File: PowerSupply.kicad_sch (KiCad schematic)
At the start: 23 parts, among them J1 Barrel_Jack, SW1 SW_SPST, U1 LM7812_TO220, U2 LM7912_TO220, U3 LM7805_TO220

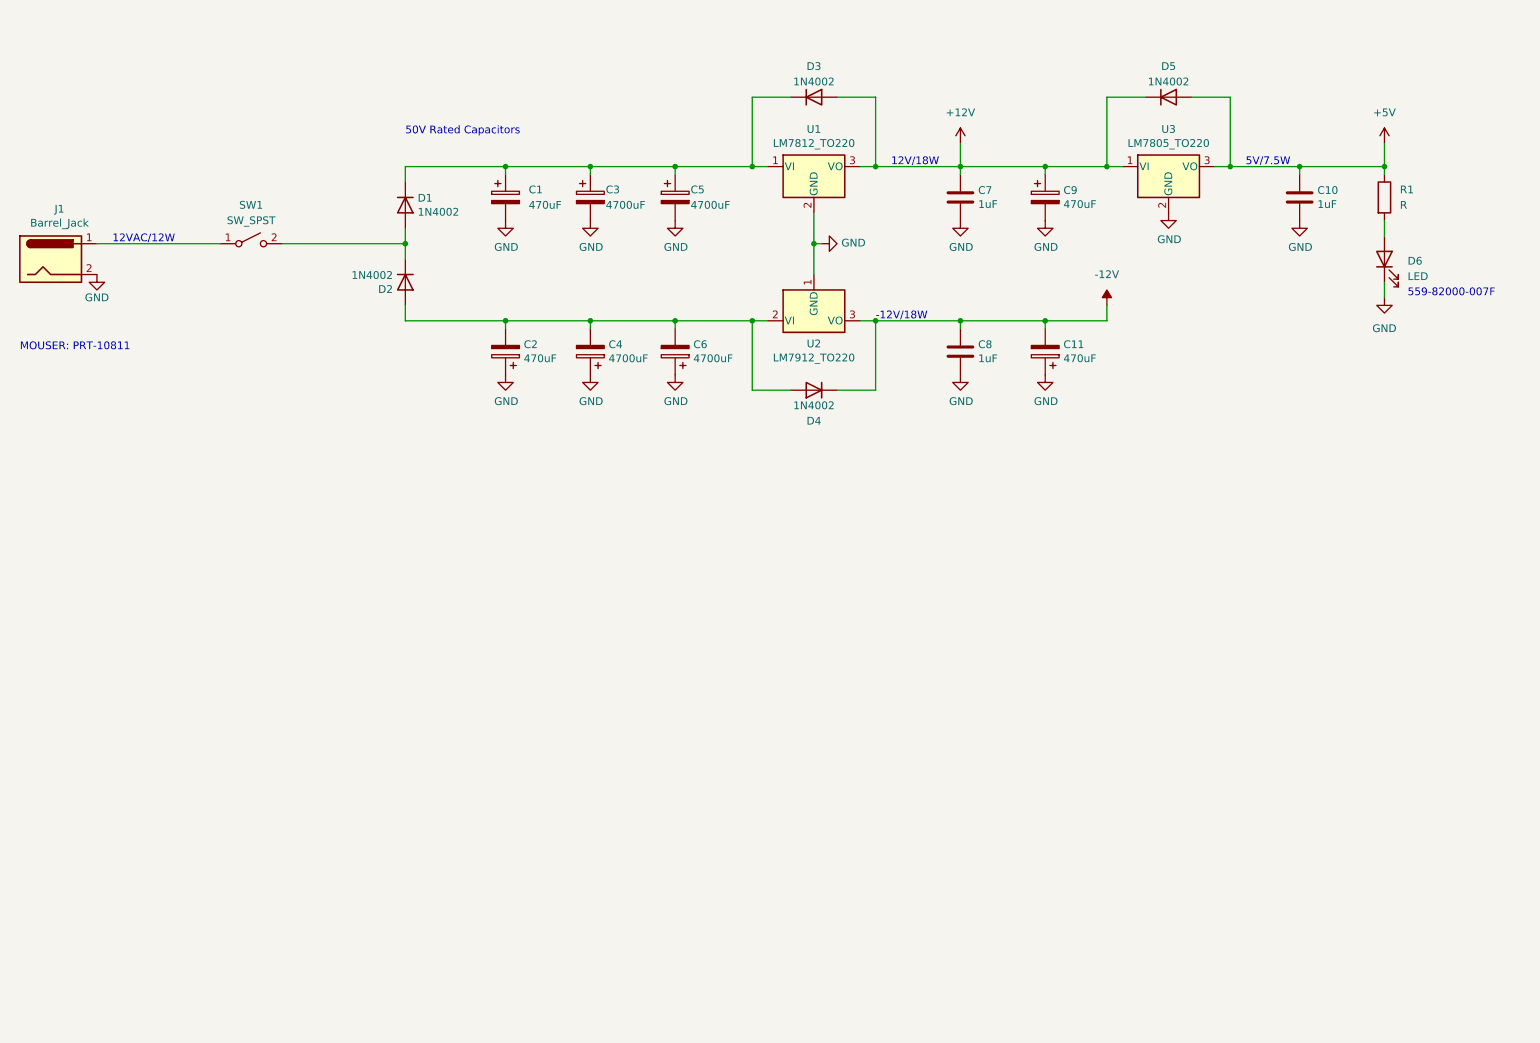
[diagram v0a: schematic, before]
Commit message: more uFs
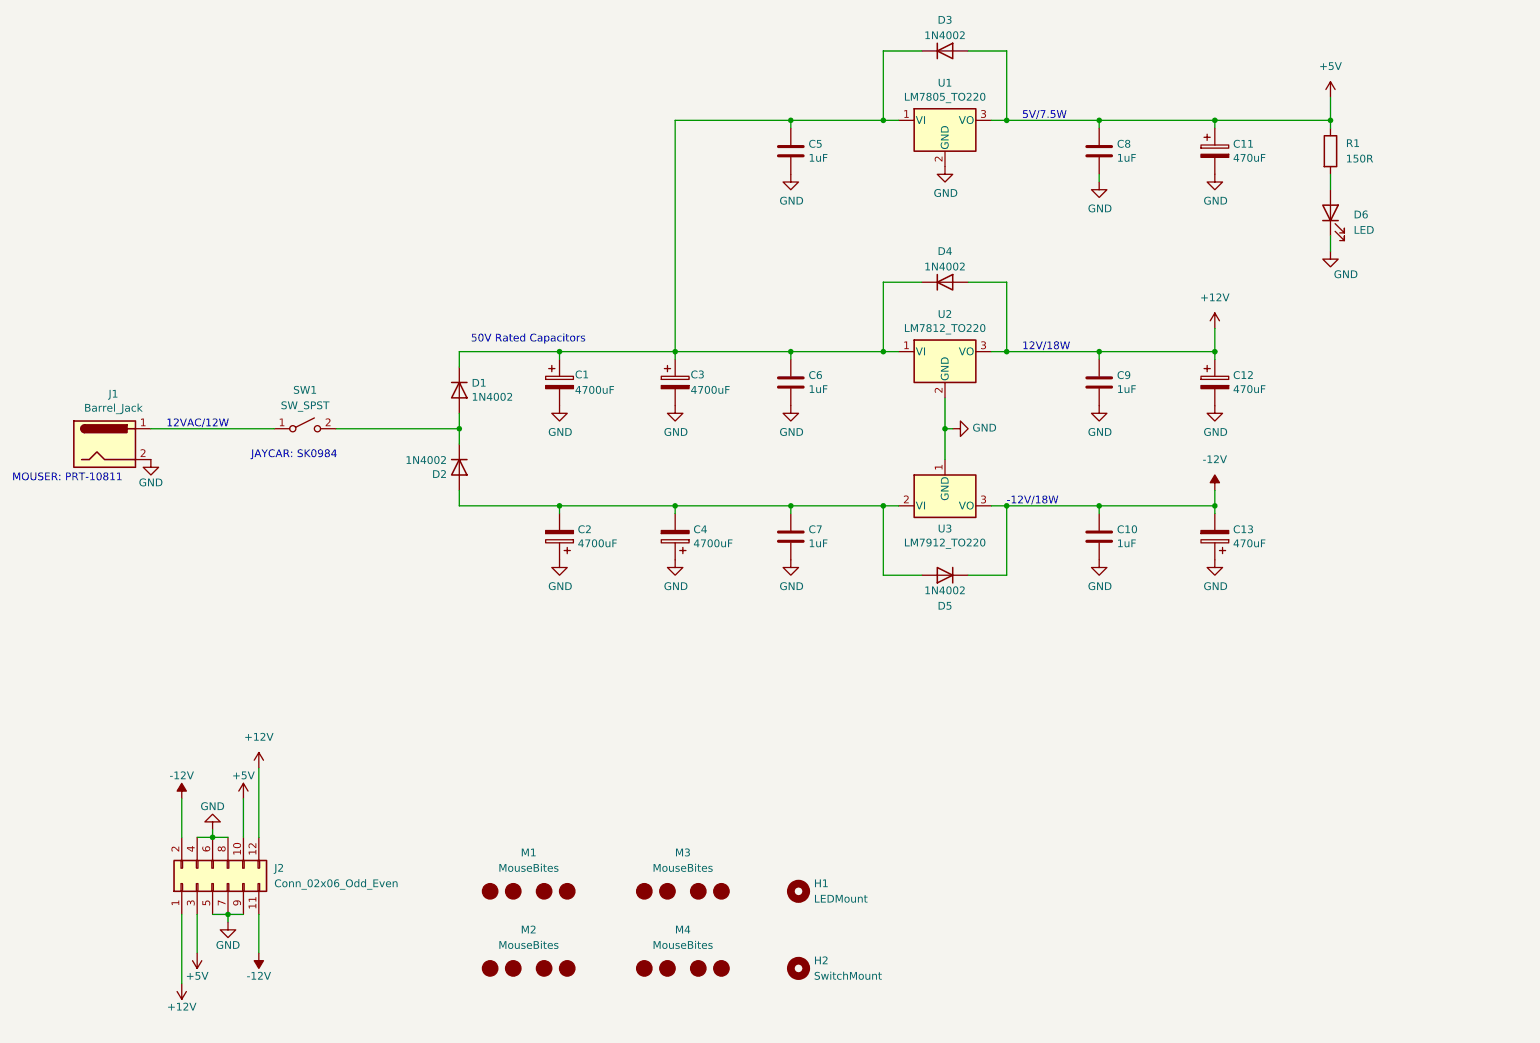
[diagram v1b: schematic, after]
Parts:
- removed C1: 470uF, Capacitor_THT:CP_Radial_D10.0mm_P5.00mm, symbol Device:CP
- removed C5, C6: 4700uF, Capacitor_THT:CP_Radial_D22.0mm_P10.00mm_SnapIn, symbol Device:CP
- added C11: 470uF, Capacitor_THT:CP_Radial_D10.0mm_P5.00mm, symbol Device:CP
- added C3: 4700uF, Capacitor_THT:CP_Radial_D22.0mm_P10.00mm_SnapIn, symbol Device:CP
- added C5, C6, C7: 1uF, Capacitor_SMD:C_0805_2012Metric_Pad1.18x1.45mm_HandSolder, symbol Device:C
- added H1: LEDMount, Synth:PowerLEDMount, symbol Mechanical:MountingHole
- added H2: SwitchMount, Synth:SwitchMount, symbol Mechanical:MountingHole
- added J2: Conn_02x06_Odd_Even, Connector_IDC:IDC-Header_2x06_P2.54mm_Vertical, symbol Connector_Generic:Conn_02x06_Odd_Even
- added M1, M2, M3, M4: MouseBites, Panelization:mouse-bite-5mm-slot, symbol Synth:MouseBites
- C2: value 470uF -> 4700uF; footprint Capacitor_THT:CP_Radial_D10.0mm_P5.00mm -> Capacitor_THT:CP_Radial_D22.0mm_P10.00mm_SnapIn
- J1: footprint (none) -> Synth:BarrelJack
- R1: value R -> 150R
- renumbered C3 to C1, C8 to C10, C9 to C12, C11 to C13, C10 to C8, C7 to C9, D5 to D3, D3 to D4, D4 to D5, U3 to U1, U1 to U2, U2 to U3
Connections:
- net +12V: now also J2.1 (Pin_1), J2.12 (Pin_12); no longer D3.1 (K), U1.1 (VI)
- net +5V: now also C11.1, J2.10 (Pin_10), J2.3 (Pin_3)
- net -12V: now also J2.11 (Pin_11), J2.2 (Pin_2)
- net GND: now also C11.2, C3.2, C5.2, C6.2, C7.2, J2.4 (Pin_4), J2.5 (Pin_5), J2.6 (Pin_6), J2.7 (Pin_7), J2.8 (Pin_8), J2.9 (Pin_9)
- net at C1.1, D1.1 (K), D4.1 (K)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: now also D3.1 (K), U1.1 (VI), C3.1, C5.1, C6.1
- net at C2.2, C4.2, D2.2 (A)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: now also C7.1
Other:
- note added: "JAYCAR: SK0984"
- note removed: "559-82000-007F"
- moved on the sheet: C1, C10, C12, C13, C4, C8, C9, D1, D2, D3, D4, D5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

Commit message: layout started
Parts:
- added D7: 12V LED, LED_THT:LED_D5.0mm, symbol Device:LED
- added D8: -12V LED, LED_THT:LED_D5.0mm, symbol Device:LED
- added H2, H3, H4, H5: MountingHole, MountingHole:MountingHole_3.2mm_M3, symbol Mechanical:MountingHole
- added H7, H8: LEDMount, MountingHole:MountingHole_5mm, symbol Mechanical:MountingHole
- added R2, R3: 150R, Resistor_SMD:R_0805_2012Metric_Pad1.20x1.40mm_HandSolder, symbol Device:R
- D6: value LED -> 5V LED; footprint Connector_Wire:SolderWire-1sqmm_1x02_P5.4mm_D1.4mm_OD2.7mm_Relief -> LED_THT:LED_D5.0mm
- H6: renamed from H1; footprint Synth:PowerLEDMount -> MountingHole:MountingHole_5mm
- J2: footprint Connector_IDC:IDC-Header_2x06_P2.54mm_Vertical -> Synth:IDC-Header_2x06_P2.54mm_Vertical
- renumbered H2 to H1
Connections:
- net +12V: now also R2.1
- net -12V: now also R3.1
- net GND: now also D7.1 (K), D8.1 (K)
- new net: D8.2 (A), R3.2
- new net: D7.2 (A), R2.2
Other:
- note added: "JAYCAR: SK0981"
- note added: "Standoffs"
- note removed: "JAYCAR: SK0984"
- moved on the sheet: D6, H6

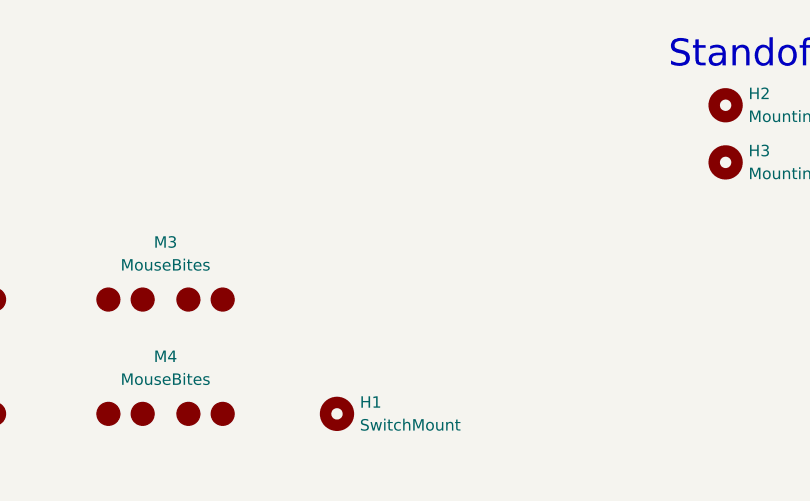
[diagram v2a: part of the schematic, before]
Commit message: Add Moutning Holes
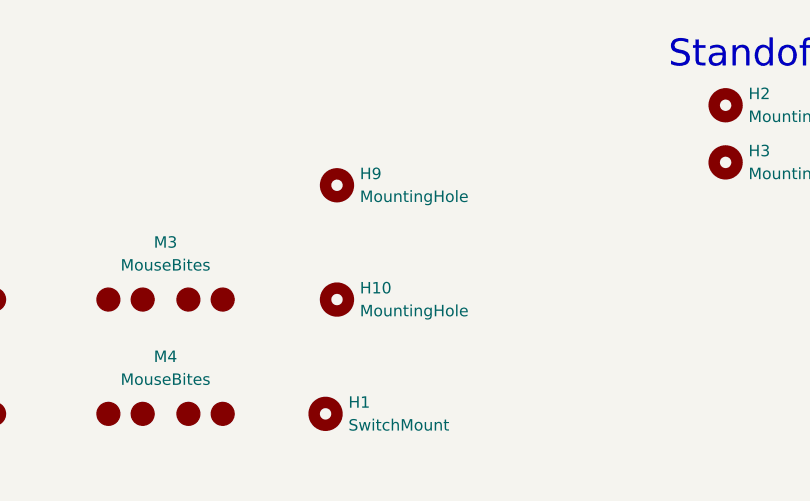
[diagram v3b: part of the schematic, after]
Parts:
- added H10, H9: MountingHole, MountingHole:MountingHole_5.3mm_M5, symbol Mechanical:MountingHole
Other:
- moved on the sheet: H1
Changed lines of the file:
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@@
     (pin "1")
   )
-  (symbol (lib_id "Mechanical:MountingHole") (at 153.67 177.8 0) (unit 1)
-    (in_bom yes) (on_board yes) (fields_autoplaced)
-    (property "Reference" "H1" (id 0) (at 156.21 176.5299 0)
-      (effects (font (size 1.27 1.27)) (justify left))
-    )
-    (property "Value" "SwitchMount" (id 1) (at 156.21 179.0699 0)
-      (effects (font (size 1.27 1.27)) (justify left))
-    )
-    (property "Footprint" "Synth:SwitchMount" (id 2) (at 153.67 177.8 0)
-      (effects (font (size 1.27 1.27)) hide)
-    )
-    (property "Datasheet" "~" (id 3) (at 153.67 177.8 0)
+  (symbol (lib_id "Mechanical:MountingHole") (at 152.4 177.8 0) (unit 1)
+    (in_bom yes) (on_board yes) (fields_autoplaced)
+    (property "Reference" "H1" (id 0) (at 154.94 176.5299 0)
+      (effects (font (size 1.27 1.27)) (justify left))
+    )
+    (property "Value" "SwitchMount" (id 1) (at 154.94 179.0699 0)
+      (effects (font (size 1.27 1.27)) (justify left))
+    )
+    (property "Footprint" "Synth:SwitchMount" (id 2) (at 152.4 177.8 0)
+      (effects (font (size 1.27 1.27)) hide)
+    )
+    (property "Datasheet" "~" (id 3) (at 152.4 177.8 0)
       (effects (font (size 1.27 1.27)) hide)
     )
@@
     (pin "2")
   )
+  (symbol (lib_id "Mechanical:MountingHole") (at 153.67 152.4 0) (unit 1)
+    (in_bom yes) (on_board yes)
+    (property "Reference" "H9" (id 0) (at 156.21 151.1299 0)
+      (effects (font (size 1.27 1.27)) (justify left))
+    )
+    (property "Value" "MountingHole" (id 1) (at 156.21 153.67 0)
+      (effects (font (size 1.27 1.27)) (justify left))
+    )
+    (property "Footprint" "MountingHole:MountingHole_5.3mm_M5" (id 2) (at 153.67 152.4 0)
+      (effects (font (size 1.27 1.27)) hide)
+    )
+    (property "Datasheet" "~" (id 3) (at 153.67 152.4 0)
+      (effects (font (size 1.27 1.27)) hide)
+    )
+  )
   (symbol (lib_id "Device:LED") (at 241.3 114.3 90) (unit 1)
     (in_bom yes) (on_board yes) (fields_autoplaced)
@@
     )
     (pin "1")
+  )
+  (symbol (lib_id "Mechanical:MountingHole") (at 153.67 165.1 0) (unit 1)
+    (in_bom yes) (on_board yes)
+    (property "Reference" "H10" (id 0) (at 156.21 163.8299 0)
+      (effects (font (size 1.27 1.27)) (justify left))
+    )
+    (property "Value" "MountingHole" (id 1) (at 156.21 166.37 0)
+      (effects (font (size 1.27 1.27)) (justify left))
+    )
+    (property "Footprint" "MountingHole:MountingHole_5.3mm_M5" (id 2) (at 153.67 165.1 0)
+      (effects (font (size 1.27 1.27)) hide)
+    )
+    (property "Datasheet" "~" (id 3) (at 153.67 165.1 0)
+      (effects (font (size 1.27 1.27)) hide)
+    )
   )
   (symbol (lib_id "Mechanical:MountingHole") (at 196.85 149.86 0) (unit 1)
@@
       (reference "H8") (unit 1) (value "LEDMount") (footprint "MountingHole:MountingHole_5mm")
     )
+    (path "/5eed9f9e-2bc4-4891-8681-4cbcd40ee44c"
+      (reference "H9") (unit 1) (value "MountingHole") (footprint "MountingHole:MountingHole_5.3mm_M5")
+    )
+    (path "/a013b01d-67ea-4b0c-8baa-9870788db576"
+      (reference "H10") (unit 1) (value "MountingHole") (footprint "MountingHole:MountingHole_5.3mm_M5")
+    )
     (path "/00000000-0000-0000-0000-0000606aa221"

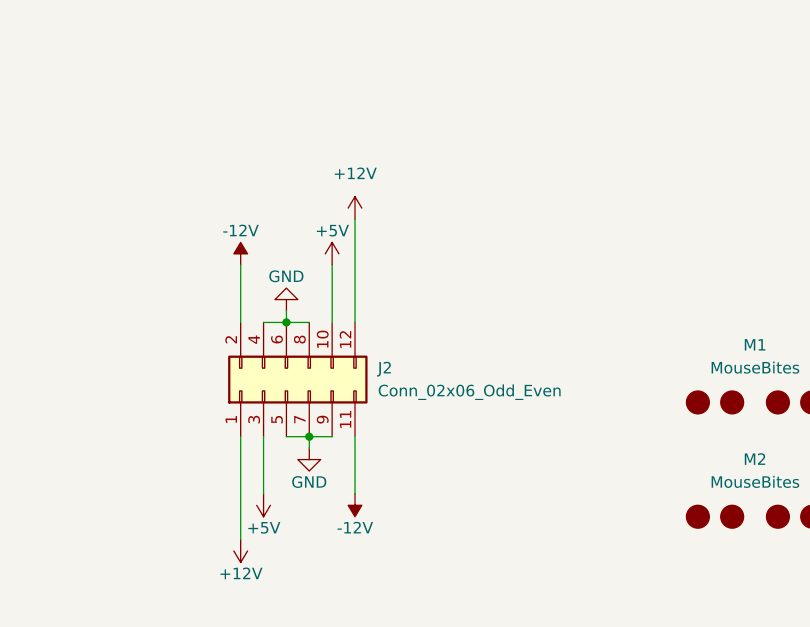
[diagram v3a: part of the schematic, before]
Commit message: Changed IDC to 2x5
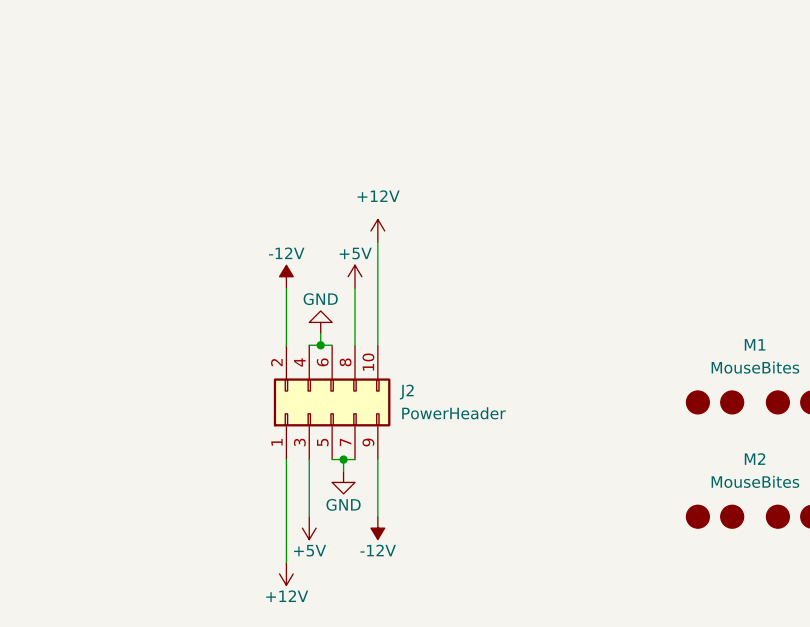
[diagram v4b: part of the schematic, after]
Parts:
- removed J2: Conn_02x06_Odd_Even, Synth:IDC-Header_2x06_P2.54mm_Vertical, symbol Connector_Generic:Conn_02x06_Odd_Even
- added J2: PowerHeader, Connector_IDC:IDC-Header_2x05_P2.54mm_Vertical, symbol Connector_Generic:Conn_02x05_Odd_Even
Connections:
- net +12V: now also J2.1 (Pin_1), J2.10 (Pin_10)
- net +5V: now also J2.3 (Pin_3), J2.8 (Pin_8)
- net -12V: now also J2.2 (Pin_2), J2.9 (Pin_9)
- net GND: now also J2.4 (Pin_4), J2.5 (Pin_5), J2.6 (Pin_6), J2.7 (Pin_7)
